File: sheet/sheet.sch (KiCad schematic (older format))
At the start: 35 parts

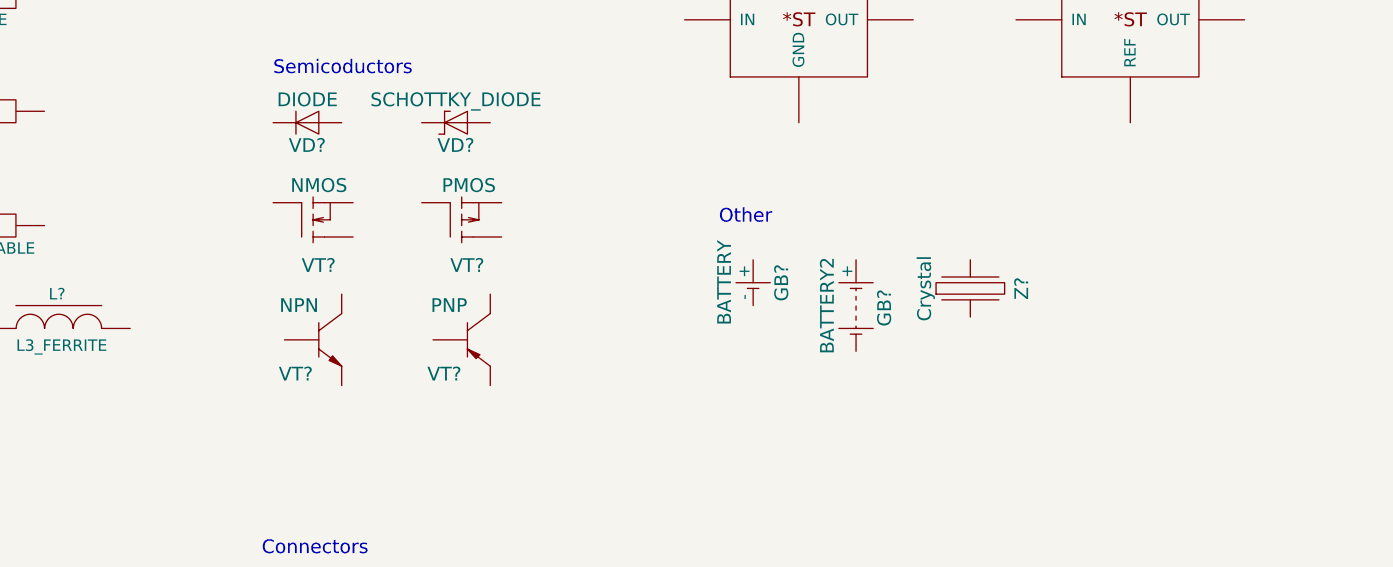
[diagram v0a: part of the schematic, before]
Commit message: Add transistors version without circle
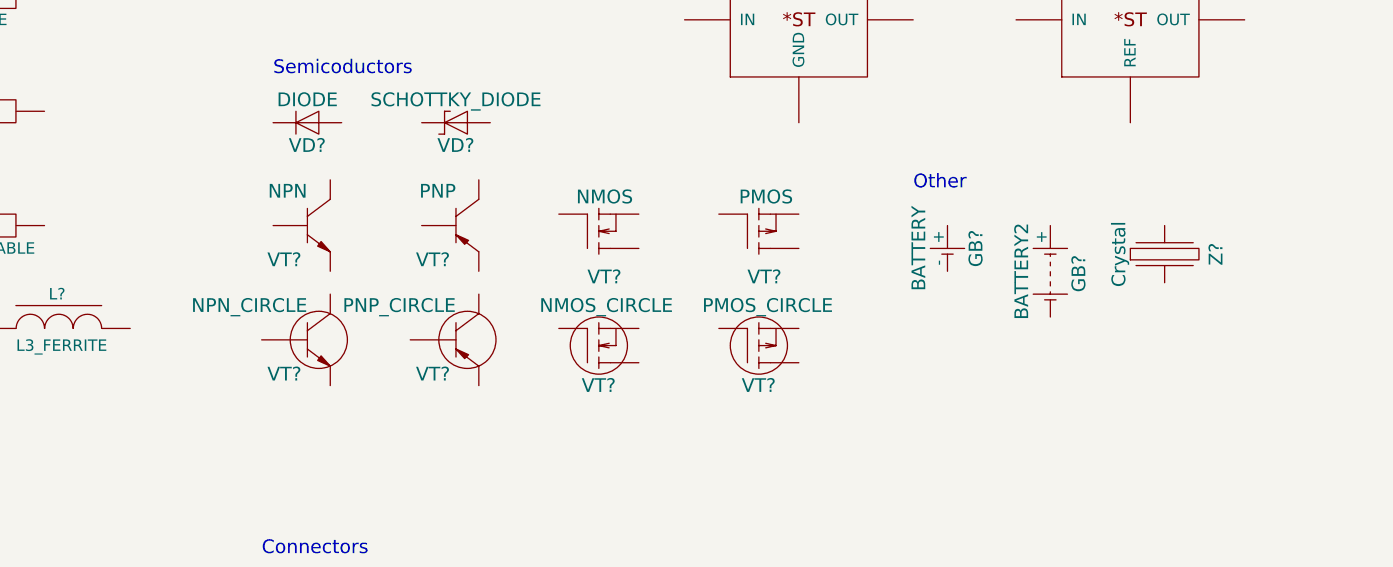
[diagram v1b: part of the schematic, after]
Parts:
- added VT?: NMOS_CIRCLE, symbol NMOS_CIRCLE
- added VT?: PMOS_CIRCLE, symbol PMOS_CIRCLE
- added VT?: NPN_CIRCLE, symbol NPN_CIRCLE
- added VT?: PNP_CIRCLE, symbol PNP_CIRCLE
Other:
- moved on the sheet: GB?, VT?, Z?
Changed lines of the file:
@@
 L NMOS VT?
 U 1 1 55D9AF68
+P 4300 2700
+F 0 "VT?" H 4425 2525 60  0000 R CNN
+F 1 "NMOS" H 4475 2875 60  0000 R CNN
+F 2 "" H 4300 2700 60  0000 C CNN
+F 3 "" H 4300 2700 60  0000 C CNN
+	1    4300 2700
+	1    0    0    -1
+$EndComp
+$Comp
+L PMOS VT?
+U 1 1 55D9AFE5
+P 5000 2700
+F 0 "VT?" H 5125 2525 60  0000 R CNN
+F 1 "PMOS" H 5175 2875 60  0000 R CNN
+F 2 "" H 5000 2700 60  0000 C CNN
+F 3 "" H 5000 2700 60  0000 C CNN
+	1    5000 2700
+	1    0    0    -1
+$EndComp
+$Comp
+L NPN VT?
+U 1 1 55D9B10B
 P 3050 2650
-F 0 "VT?" H 3175 2475 60  0000 R CNN
-F 1 "NMOS" H 3225 2825 60  0000 R CNN
+F 0 "VT?" H 3025 2500 60  0000 R CNN
+F 1 "NPN" H 3050 2800 60  0000 R CNN
 F 2 "" H 3050 2650 60  0000 C CNN
 F 3 "" H 3050 2650 60  0000 C CNN
@@
 $EndComp
 $Comp
-L PMOS VT?
-U 1 1 55D9AFE5
+L PNP VT?
+U 1 1 55D9B160
 P 3700 2650
-F 0 "VT?" H 3825 2475 60  0000 R CNN
-F 1 "PMOS" H 3875 2825 60  0000 R CNN
+F 0 "VT?" H 3675 2500 60  0000 R CNN
+F 1 "PNP" H 3700 2800 60  0000 R CNN
 F 2 "" H 3700 2650 60  0000 C CNN
 F 3 "" H 3700 2650 60  0000 C CNN
 	1    3700 2650
-	1    0    0    -1
-$EndComp
-$Comp
-L NPN VT?
-U 1 1 55D9B10B
-P 3100 3150
-F 0 "VT?" H 3075 3000 60  0000 R CNN
-F 1 "NPN" H 3100 3300 60  0000 R CNN
-F 2 "" H 3100 3150 60  0000 C CNN
-F 3 "" H 3100 3150 60  0000 C CNN
-	1    3100 3150
-	1    0    0    -1
-$EndComp
-$Comp
-L PNP VT?
-U 1 1 55D9B160
-P 3750 3150
-F 0 "VT?" H 3725 3000 60  0000 R CNN
-F 1 "PNP" H 3750 3300 60  0000 R CNN
-F 2 "" H 3750 3150 60  0000 C CNN
-F 3 "" H 3750 3150 60  0000 C CNN
-	1    3750 3150
 	1    0    0    -1
 $EndComp
@@
 L BATTERY GB?
 U 1 1 55D9BEA9
-P 5000 2900
-F 0 "GB?" V 5125 2900 60  0000 C CNN
-F 1 "BATTERY" V 4875 2900 60  0000 C CNN
-F 2 "" H 5000 2900 60  0000 C CNN
-F 3 "" H 5000 2900 60  0000 C CNN
-	1    5000 2900
+P 5850 2750
+F 0 "GB?" V 5975 2750 60  0000 C CNN
+F 1 "BATTERY" V 5725 2750 60  0000 C CNN
+F 2 "" H 5850 2750 60  0000 C CNN
+F 3 "" H 5850 2750 60  0000 C CNN
+	1    5850 2750
 	1    0    0    -1
 $EndComp
@@
 L BATTERY2 GB?
 U 1 1 55D9BF58
-P 5450 3000
-F 0 "GB?" V 5575 2990 60  0000 C CNN
-F 1 "BATTERY2" V 5325 3000 60  0000 C CNN
-F 2 "" H 5450 3000 60  0000 C CNN
-F 3 "" H 5450 3000 60  0000 C CNN
-	1    5450 3000
+P 6300 2850
+F 0 "GB?" V 6425 2840 60  0000 C CNN
+F 1 "BATTERY2" V 6175 2850 60  0000 C CNN
+F 2 "" H 6300 2850 60  0000 C CNN
+F 3 "" H 6300 2850 60  0000 C CNN
+	1    6300 2850
 	1    0    0    -1
 $EndComp
@@
 L Crystal Z?
 U 1 1 55D9C112
-P 5950 2950
-F 0 "Z?" V 6175 2975 60  0000 C CNN
-F 1 "Crystal" V 5750 2975 60  0000 C CNN
-F 2 "" H 5950 2950 60  0000 C CNN
-F 3 "" H 5950 2950 60  0000 C CNN
-	1    5950 2950
-	1    0    0    -1
-$EndComp
-Text Notes 4850 2650 0    60   ~ 0
+P 6800 2800
+F 0 "Z?" V 7025 2825 60  0000 C CNN
+F 1 "Crystal" V 6600 2825 60  0000 C CNN
+F 2 "" H 6800 2800 60  0000 C CNN
+F 3 "" H 6800 2800 60  0000 C CNN
+	1    6800 2800
+	1    0    0    -1
+$EndComp
+Text Notes 5700 2500 0    60   ~ 0
 Other
 $Comp
@@
 	1    0    0    -1
 $EndComp
+$Comp
+L NMOS_CIRCLE VT?
+U 1 1 55DAE0AB
+P 4300 3200
+F 0 "VT?" H 4400 3050 60  0000 R CNN
+F 1 "NMOS_CIRCLE" H 4650 3400 60  0000 R CNN
+F 2 "" H 4275 3225 60  0000 C CNN
+F 3 "" H 4275 3225 60  0000 C CNN
+	1    4300 3200
+	1    0    0    -1
+$EndComp
+$Comp
+L PMOS_CIRCLE VT?
+U 1 1 55DAE216
+P 5000 3200
+F 0 "VT?" H 5100 3050 60  0000 R CNN
+F 1 "PMOS_CIRCLE" H 5350 3400 60  0000 R CNN
+F 2 "" H 4975 3225 60  0000 C CNN
+F 3 "" H 4975 3225 60  0000 C CNN
+	1    5000 3200
+	1    0    0    -1
+$EndComp
+$Comp
+L NPN_CIRCLE VT?
+U 1 1 55DB069D
+P 3050 3150
+F 0 "VT?" H 3025 3000 60  0000 R CNN
+F 1 "NPN_CIRCLE" H 3050 3300 60  0000 R CNN
+F 2 "" H 3050 3150 60  0000 C CNN
+F 3 "" H 3050 3150 60  0000 C CNN
+	1    3050 3150
+	1    0    0    -1
+$EndComp
+$Comp
+L PNP_CIRCLE VT?
+U 1 1 55DB0714
+P 3700 3150
+F 0 "VT?" H 3675 3000 60  0000 R CNN
+F 1 "PNP_CIRCLE" H 3700 3300 60  0000 R CNN
+F 2 "" H 3700 3150 60  0000 C CNN
+F 3 "" H 3700 3150 60  0000 C CNN
+	1    3700 3150
+	1    0    0    -1
+$EndComp

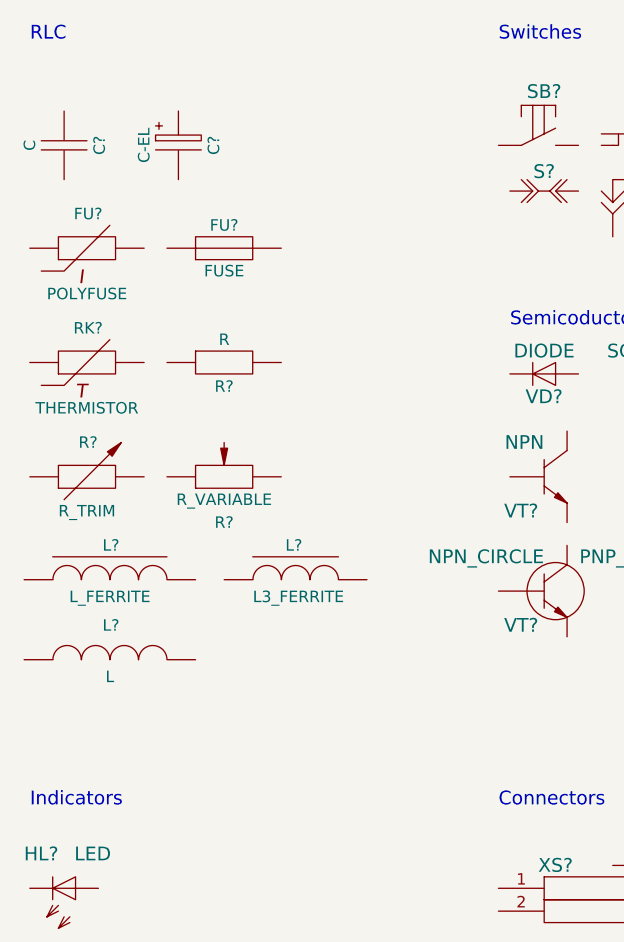
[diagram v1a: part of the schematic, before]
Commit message: Add variable and trimmer capacitors
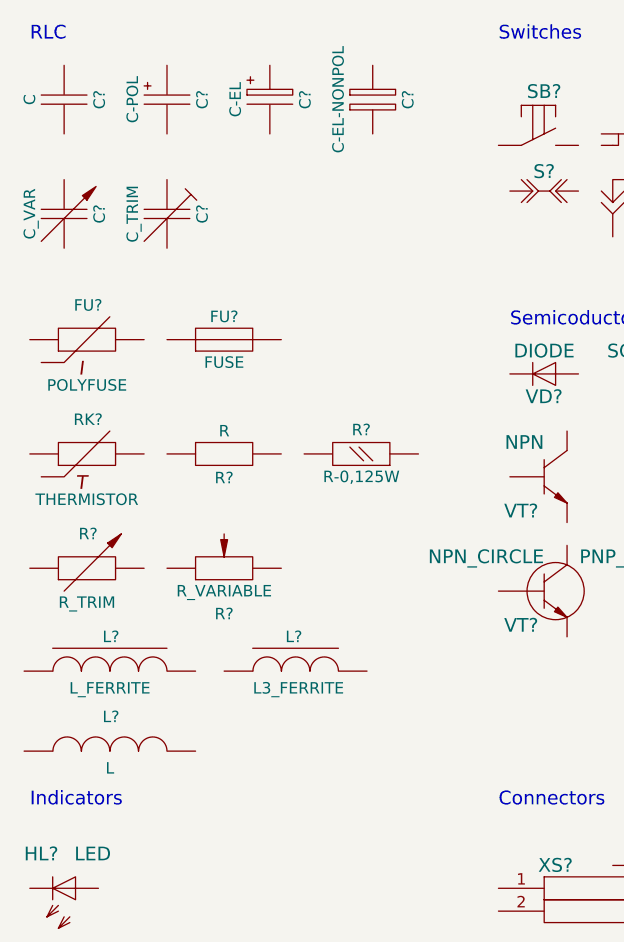
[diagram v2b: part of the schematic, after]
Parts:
- added C?: C-POL, symbol C-POL
- added C?: C-EL-NONPOL, symbol C-EL-NONPOL
- added C?: C_VAR, symbol C_VAR
- added C?: C_TRIM, symbol C_TRIM
- added R?: R-0,125W, symbol R-0,125W
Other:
- moved on the sheet: C?, FU?, L?, R?, RK?
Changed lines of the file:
@@
 L C C?
 U 1 1 55D8CA86
-P 950 1200
-F 0 "C?" V 1105 1200 50  0000 C CNN
-F 1 "C" V 800 1200 50  0000 C CNN
-F 2 "" H 950 1200 60  0000 C CNN
-F 3 "" H 950 1200 60  0000 C CNN
-	1    950  1200
+P 950 1000
+F 0 "C?" V 1105 1000 50  0000 C CNN
+F 1 "C" V 800 1000 50  0000 C CNN
+F 2 "" H 950 1000 60  0000 C CNN
+F 3 "" H 950 1000 60  0000 C CNN
+	1    950  1000
 	1    0    0    -1
 $EndComp
@@
 L C-EL C?
 U 1 1 55D8CAA7
-P 1450 1200
-F 0 "C?" V 1605 1200 50  0000 C CNN
-F 1 "C-EL" V 1300 1200 50  0000 C CNN
-F 2 "" H 1450 1200 60  0000 C CNN
-F 3 "" H 1450 1200 60  0000 C CNN
-	1    1450 1200
+P 1850 1000
+F 0 "C?" V 2005 1000 50  0000 C CNN
+F 1 "C-EL" V 1700 1000 50  0000 C CNN
+F 2 "" H 1850 1000 60  0000 C CNN
+F 3 "" H 1850 1000 60  0000 C CNN
+	1    1850 1000
 	1    0    0    -1
 $EndComp
@@
 L FUSE FU?
 U 1 1 55D8CAF1
-P 1650 1650
-F 0 "FU?" H 1650 1750 50  0000 C CNN
-F 1 "FUSE" H 1650 1550 50  0000 C CNN
-F 2 "" H 1700 1450 60  0000 C CNN
-F 3 "" H 1650 1650 60  0000 C CNN
-	1    1650 1650
+P 1650 2050
+F 0 "FU?" H 1650 2150 50  0000 C CNN
+F 1 "FUSE" H 1650 1950 50  0000 C CNN
+F 2 "" H 1700 1850 60  0000 C CNN
+F 3 "" H 1650 2050 60  0000 C CNN
+	1    1650 2050
 	1    0    0    -1
 $EndComp
@@
 L R R?
 U 1 1 55D8CB70
-P 1650 2150
-F 0 "R?" V 1755 2150 50  0000 C CNN
-F 1 "R" V 1550 2150 50  0000 C CNN
-F 2 "" H 1650 2150 60  0000 C CNN
-F 3 "" H 1650 2150 60  0000 C CNN
-	1    1650 2150
+P 1650 2550
+F 0 "R?" V 1755 2550 50  0000 C CNN
+F 1 "R" V 1550 2550 50  0000 C CNN
+F 2 "" H 1650 2550 60  0000 C CNN
+F 3 "" H 1650 2550 60  0000 C CNN
+	1    1650 2550
 	0    1    1    0
 $EndComp
@@
 L L L?
 U 1 1 55D8CBF9
-P 1150 3450
-F 0 "L?" H 1155 3600 50  0000 C CNN
-F 1 "L" H 1150 3375 50  0000 C CNN
-F 2 "" H 1075 3450 60  0000 C CNN
-F 3 "" H 1075 3450 60  0000 C CNN
-	1    1150 3450
+P 1150 3850
+F 0 "L?" H 1155 4000 50  0000 C CNN
+F 1 "L" H 1150 3775 50  0000 C CNN
+F 2 "" H 1075 3850 60  0000 C CNN
+F 3 "" H 1075 3850 60  0000 C CNN
+	1    1150 3850
 	1    0    0    -1
 $EndComp
@@
 L L3_FERRITE L?
 U 1 1 55D8CC6C
-P 1950 3100
-F 0 "L?" H 1955 3250 50  0000 C CNN
-F 1 "L3_FERRITE" H 1975 3025 50  0000 C CNN
-F 2 "" H 1950 3100 60  0000 C CNN
-F 3 "" H 1950 3100 60  0000 C CNN
-	1    1950 3100
+P 1950 3500
+F 0 "L?" H 1955 3650 50  0000 C CNN
+F 1 "L3_FERRITE" H 1975 3425 50  0000 C CNN
+F 2 "" H 1950 3500 60  0000 C CNN
+F 3 "" H 1950 3500 60  0000 C CNN
+	1    1950 3500
 	1    0    0    -1
 $EndComp
@@
 L L_FERRITE L?
 U 1 1 55D8CCBD
-P 1150 3100
-F 0 "L?" H 1155 3250 50  0000 C CNN
-F 1 "L_FERRITE" H 1150 3025 50  0000 C CNN
-F 2 "" H 1075 3100 60  0000 C CNN
-F 3 "" H 1075 3100 60  0000 C CNN
-	1    1150 3100
+P 1150 3500
+F 0 "L?" H 1155 3650 50  0000 C CNN
+F 1 "L_FERRITE" H 1150 3425 50  0000 C CNN
+F 2 "" H 1075 3500 60  0000 C CNN
+F 3 "" H 1075 3500 60  0000 C CNN
+	1    1150 3500
 	1    0    0    -1
 $EndComp
@@
 L POLYFUSE FU?
 U 1 1 55D8CD66
-P 1050 1650
-F 0 "FU?" H 1055 1800 50  0000 C CNN
-F 1 "POLYFUSE" H 1050 1450 50  0000 C CNN
-F 2 "" H 1050 1650 60  0000 C CNN
-F 3 "" H 1050 1650 60  0000 C CNN
-	1    1050 1650
+P 1050 2050
+F 0 "FU?" H 1055 2200 50  0000 C CNN
+F 1 "POLYFUSE" H 1050 1850 50  0000 C CNN
+F 2 "" H 1050 2050 60  0000 C CNN
+F 3 "" H 1050 2050 60  0000 C CNN
+	1    1050 2050
 	1    0    0    -1
 $EndComp
@@
 L THERMISTOR RK?
 U 1 1 55D8CDF1
-P 1050 2150
-F 0 "RK?" H 1055 2300 50  0000 C CNN
-F 1 "THERMISTOR" H 1050 1950 50  0000 C CNN
-F 2 "" H 1050 2150 60  0000 C CNN
-F 3 "" H 1050 2150 60  0000 C CNN
-	1    1050 2150
+P 1050 2550
+F 0 "RK?" H 1055 2700 50  0000 C CNN
+F 1 "THERMISTOR" H 1050 2350 50  0000 C CNN
+F 2 "" H 1050 2550 60  0000 C CNN
+F 3 "" H 1050 2550 60  0000 C CNN
+	1    1050 2550
 	1    0    0    -1
 $EndComp
@@
 L R_TRIM R?
 U 1 1 55D8CE2C
-P 1050 2650
-F 0 "R?" H 1055 2800 50  0000 C CNN
-F 1 "R_TRIM" H 1050 2500 50  0000 C CNN
-F 2 "" H 1050 2650 60  0000 C CNN
-F 3 "" H 1050 2650 60  0000 C CNN
-	1    1050 2650
+P 1050 3050
+F 0 "R?" H 1055 3200 50  0000 C CNN
+F 1 "R_TRIM" H 1050 2900 50  0000 C CNN
+F 2 "" H 1050 3050 60  0000 C CNN
+F 3 "" H 1050 3050 60  0000 C CNN
+	1    1050 3050
 	1    0    0    -1
 $EndComp
@@
 L R_VARIABLE R?
 U 1 1 55D8CE7D
-P 1650 2650
-F 0 "R?" H 1650 2450 50  0000 C CNN
-F 1 "R_VARIABLE" H 1650 2550 50  0000 C CNN
-F 2 "" H 1650 2650 60  0000 C CNN
-F 3 "" H 1650 2650 60  0000 C CNN
-	1    1650 2650
+P 1650 3050
+F 0 "R?" H 1650 2850 50  0000 C CNN
+F 1 "R_VARIABLE" H 1650 2950 50  0000 C CNN
+F 2 "" H 1650 3050 60  0000 C CNN
+F 3 "" H 1650 3050 60  0000 C CNN
+	1    1650 3050
 	1    0    0    -1
 $EndComp
@@
 	1    0    0    -1
 $EndComp
+$Comp
+L C-POL C?
+U 1 1 55DB600C
+P 1400 1000
+F 0 "C?" V 1555 1000 50  0000 C CNN
+F 1 "C-POL" V 1250 1000 50  0000 C CNN
+F 2 "" H 1400 1000 60  0000 C CNN
+F 3 "" H 1400 1000 60  0000 C CNN
+	1    1400 1000
+	1    0    0    -1
+$EndComp
+$Comp
+L C-EL-NONPOL C?
+U 1 1 55DB73DF
+P 2300 1000
+F 0 "C?" V 2455 1000 50  0000 C CNN
+F 1 "C-EL-NONPOL" V 2150 1000 50  0000 C CNN
+F 2 "" H 2300 1000 60  0000 C CNN
+F 3 "" H 2300 1000 60  0000 C CNN
+	1    2300 1000
+	1    0    0    -1
+$EndComp
+$Comp
+L R-0,125W R?
+U 1 1 55DB7D86
+P 2250 2550
+F 0 "R?" V 2355 2550 50  0000 C CNN
+F 1 "R-0,125W" V 2150 2550 50  0000 C CNN
+F 2 "" H 2250 2550 60  0000 C CNN
+F 3 "" H 2250 2550 60  0000 C CNN
+	1    2250 2550
+	0    -1   -1   0
+$EndComp
+$Comp
+L C_VAR C?
+U 1 1 55DBBA9B
+P 950 1500
+F 0 "C?" V 1105 1500 50  0000 C CNN
+F 1 "C_VAR" V 800 1500 50  0000 C CNN
+F 2 "" H 950 1500 60  0000 C CNN
+F 3 "" H 950 1500 60  0000 C CNN
+	1    950  1500
+	1    0    0    -1
+$EndComp
+$Comp
+L C_TRIM C?
+U 1 1 55DC565E
+P 1400 1500
+F 0 "C?" V 1555 1500 50  0000 C CNN
+F 1 "C_TRIM" V 1250 1500 50  0000 C CNN
+F 2 "" H 1400 1500 60  0000 C CNN
+F 3 "" H 1400 1500 60  0000 C CNN
+	1    1400 1500
+	1    0    0    -1
+$EndComp
